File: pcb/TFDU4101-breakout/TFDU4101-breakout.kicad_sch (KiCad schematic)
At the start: 2 parts, among them J1 Conn_01x08_Pin, U1 TFDU4101-TR3

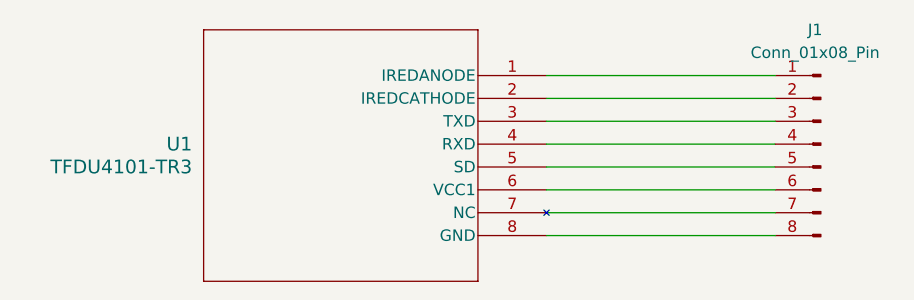
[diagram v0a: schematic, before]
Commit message: Alternate breakout down to 4 pins, optional passives
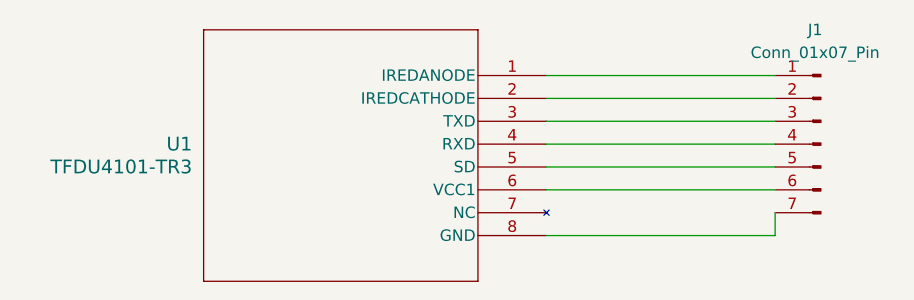
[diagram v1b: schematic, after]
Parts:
- J1: value Conn_01x08_Pin -> Conn_01x07_Pin; symbol Connector:Conn_01x08_Pin -> Connector:Conn_01x07_Pin
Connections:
- net at J1.7 (Pin_7): now also U1.8 (GND); no longer U1.7 (NC)
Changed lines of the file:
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@@
+	(wire
+		(pts
+			(xy 151.13 53.34) (xy 151.13 55.88)
+		)
+		(stroke
+			(width 0)
+			(type default)
+		)
+	)
 	(wire
 		(pts
@@
 		)
 	)
-	(wire
-		(pts
-			(xy 125.73 53.34) (xy 151.13 53.34)
-		)
-		(stroke
-			(width 0)
-			(type default)
-		)
-	)
 	(symbol
-		(lib_id "Connector:Conn_01x08_Pin")
+		(lib_id "Connector:Conn_01x07_Pin")
 		(at 156.21 45.72 0)
 		(mirror y)
@@
 			)
 		)
-		(property "Value" "Conn_01x08_Pin"
+		(property "Value" "Conn_01x07_Pin"
 			(at 155.575 35.56 0)
 			(effects
@@
 			)
 		)
-		(property "Description" "Generic connector, single row, 01x08, script generated"
+		(property "Description" "Generic connector, single row, 01x07, script generated"
 			(at 156.21 45.72 0)
 			(effects
@@
 		(pin "1"
 		)
-		(pin "8"
-		)
 		(pin "4"
